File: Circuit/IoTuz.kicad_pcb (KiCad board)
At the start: 2 copper layers, 150 x 95 mm, 103 parts, among them J1 Jack.3.5mm-Mono, P1 ALLIGATOR_X39, P2 BATTERY, P3 USB_5PIN_SHELL, P4 LED_1, P5 LED_2, P8 IRReceiver, Q1 S8050, Q2 S8050, Q202 FDN340P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

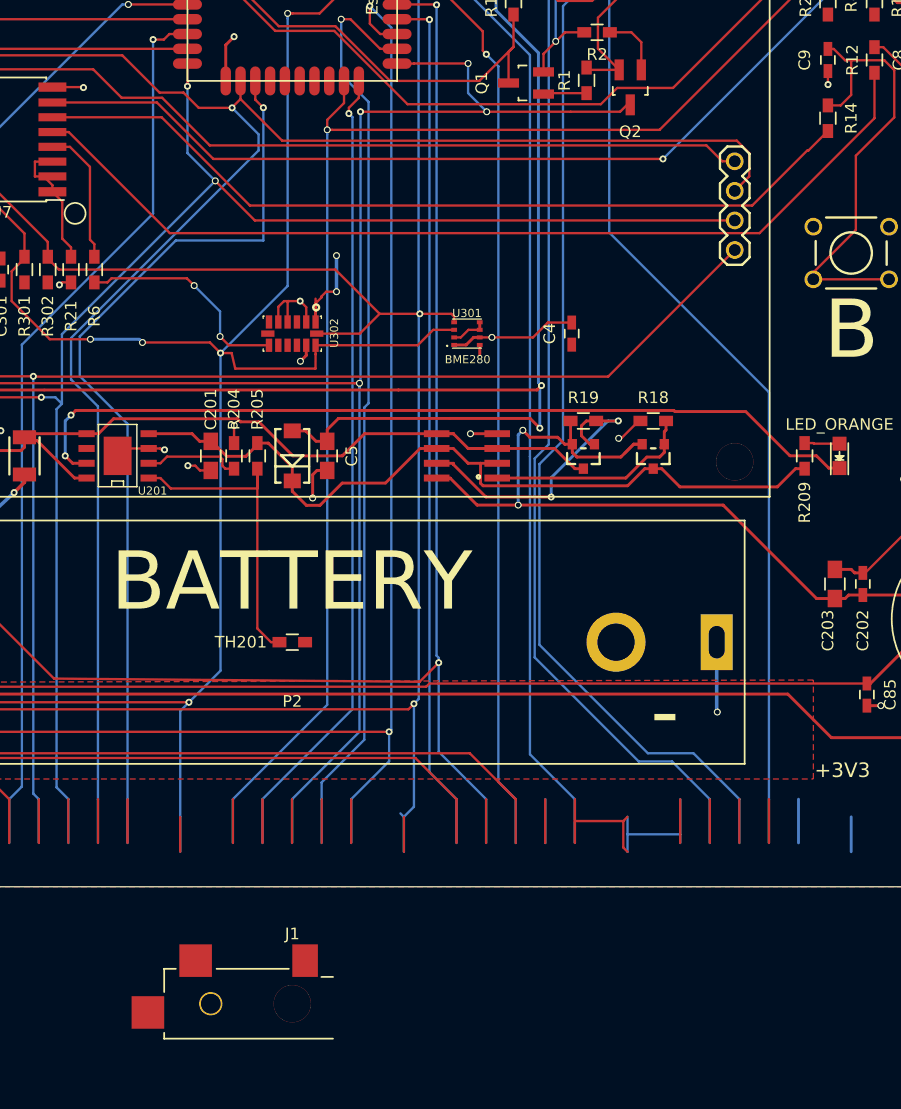
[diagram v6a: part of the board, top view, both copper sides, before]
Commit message: BOM changes to fix #15, fix #24.
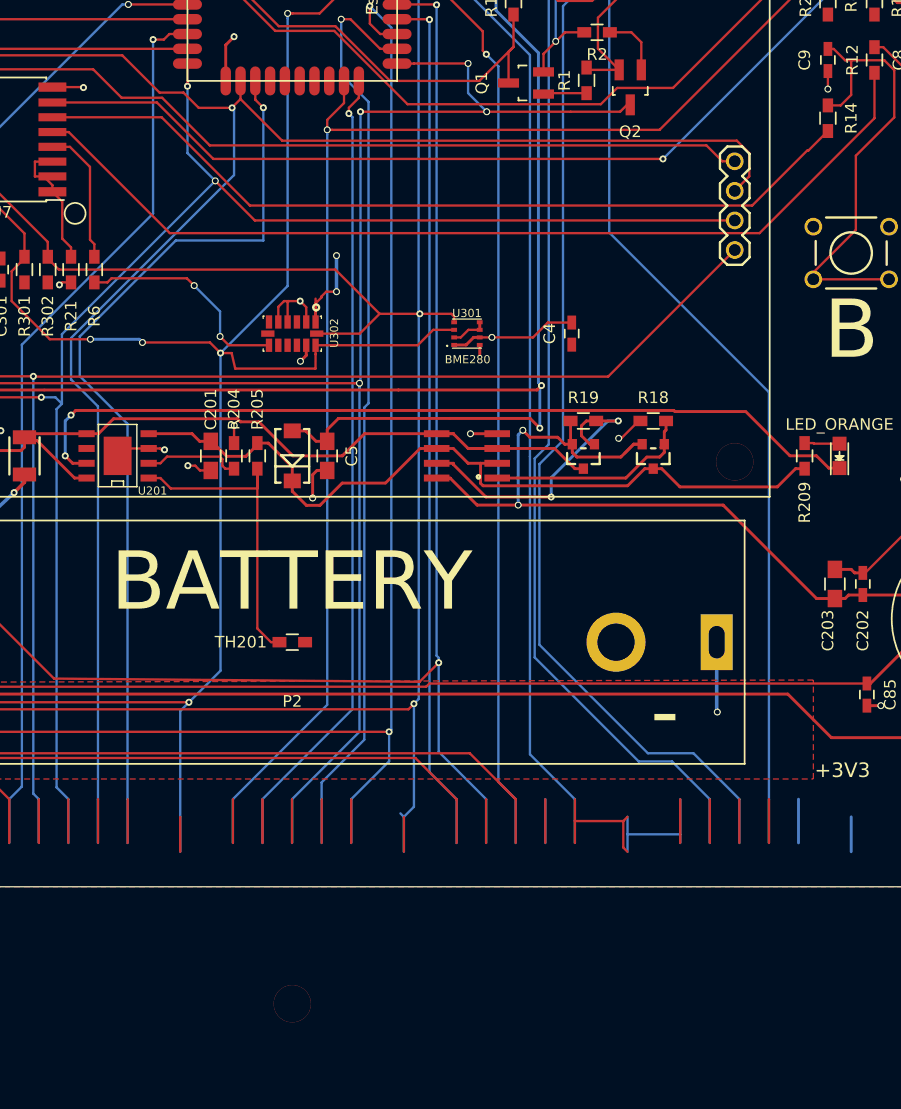
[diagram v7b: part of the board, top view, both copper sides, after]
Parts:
- removed J1: Jack.3.5mm-Mono, libs:3.5mmMonoTSJack.MJ-3523-SMT.Switch
- R16: value 22R -> 22R 1/4W
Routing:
- net /IO13: track 196.5 -> 194.7 mm
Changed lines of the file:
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@@
   (general
     (links 391)
-    (no_connects 55)
+    (no_connects 51)
     (area 49.949999 54.949999 200.050001 150.050001)
     (thickness 1.6)
     (drawings 219)
-    (tracks 1398)
+    (tracks 1397)
     (zones 0)
-    (modules 103)
+    (modules 102)
     (nets 122)
   )
@@
       (effects (font (size 1 1) (thickness 0.15)))
     )
-    (fp_text value 22R (at 0 1.9 90) (layer F.Fab)
+    (fp_text value "22R 1/4W" (at 0 1.9 90) (layer F.Fab)
       (effects (font (size 1 1) (thickness 0.15)))
     )
@@
     )
   )
-  (module libs:3.5mmMonoTSJack.MJ-3523-SMT.Switch (layer F.Cu)
-    (at 125 160.050001)
-    (fp_text reference J1 (at 0 -6) (layer F.SilkS)
-      (effects (font (size 1 1) (thickness 0.15)))
-    )
-    (fp_text value Jack.3.5mm-Mono (at 0 4.75) (layer F.Fab)
-      (effects (font (size 1 1) (thickness 0.15)))
-    )
-    (fp_text user "Keep Clear - Insertion Point" (at 18 0) (layer Cmts.User)
-      (effects (font (size 1 1) (thickness 0.15)))
-    )
-    (fp_line (start 3.5 -3.25) (end 3.5 3.25) (layer Cmts.User) (width 0.15))
-    (fp_text user Overhang (at 4.75 0 90) (layer Cmts.User)
-      (effects (font (size 1 1) (thickness 0.15)))
-    )
-    (fp_line (start 6.25 3.25) (end -11.25 3.25) (layer F.CrtYd) (width 0.15))
-    (fp_line (start 6.25 -3.25) (end 6.25 3.25) (layer F.CrtYd) (width 0.15))
-    (fp_line (start -11.25 -3.25) (end 6.25 -3.25) (layer F.CrtYd) (width 0.15))
-    (fp_line (start -11.25 3.25) (end -11.25 -3.25) (layer F.CrtYd) (width 0.15))
-    (fp_line (start 3.5 -2.3) (end 2.5 -2.3) (layer F.SilkS) (width 0.15))
-    (fp_line (start -6.5 -3) (end -0.3 -3) (layer F.SilkS) (width 0.15))
-    (fp_line (start -11 -3) (end -10 -3) (layer F.SilkS) (width 0.15))
-    (fp_line (start -11 -1) (end -11 -3) (layer F.SilkS) (width 0.15))
-    (fp_line (start -11 3) (end -11 2.5) (layer F.SilkS) (width 0.15))
-    (fp_line (start 3.5 3) (end -11 3) (layer F.SilkS) (width 0.15))
-    (pad "" thru_hole circle (at 0 0) (size 2 2) (drill 1.7) (layers *.Cu *.Mask))
-    (pad "" thru_hole circle (at -7 0) (size 2 2) (drill 1.7) (layers *.Cu *.Mask))
-    (pad 1 smd rect (at 1.1 -3.7) (size 2.2 2.8) (layers F.Cu F.Paste F.Mask)
-      (net 2 GND))
-    (pad 2 smd rect (at -8.3 -3.7) (size 2.8 2.8) (layers F.Cu F.Paste F.Mask)
-      (net 99 /MonoAudioOut))
-    (pad 10 smd rect (at -12.4 0.75) (size 2.8 2.8) (layers F.Cu F.Paste F.Mask)
-      (net 94 "Net-(J1-Pad10)"))
-  )
   (gr_text "© 2016 Robert Powers\nLicense TAPR OHL v1.0" (at 70 136.5) (layer F.SilkS)
     (effects (font (size 1.25 1.25) (thickness 0.25)))
@@
   (segment (start 86 62.9) (end 85.9004 62.9) (width 0.2032) (layer F.Cu) (net 1) (status 30))
   (segment (start 100 95.9) (end 100 96.05) (width 0.2032) (layer F.Cu) (net 1) (status 30))
+  (via (at 171 81.5) (size 0.6) (drill 0.4) (layers F.Cu B.Cu) (net 2))
+  (segment (start 171 81.5) (end 171 79.95) (width 0.2032) (layer F.Cu) (net 2))
   (segment (start 145.675 102.825) (end 146.95 101.55) (width 0.2032) (layer F.Cu) (net 2))
   (segment (start 146.95 101.55) (end 149 101.55) (width 0.2032) (layer F.Cu) (net 2))
@@
   (via (at 62.5652 114.012) (size 0.6) (layers F.Cu B.Cu) (net 2))
   (via (at 193.292 133.738) (size 0.6) (layers F.Cu B.Cu) (net 2))
-  (via (at 171.012 81.1125) (size 0.6) (layers F.Cu B.Cu) (net 2))
   (via (at 177.602 77.1926) (size 0.6) (layers F.Cu B.Cu) (net 2))
   (via (at 60.6152 98.9357) (size 0.6) (layers F.Cu B.Cu) (net 2))
@@
   (segment (start 192.68 134.05) (end 192.993 133.738) (width 0.2032) (layer F.Cu) (net 2))
   (segment (start 192 134.05) (end 192.68 134.05) (width 0.2032) (layer F.Cu) (net 2) (status 10))
-  (segment (start 171 81.1004) (end 171 79.95) (width 0.2032) (layer F.Cu) (net 2) (status 20))
-  (segment (start 171.012 81.1125) (end 171 81.1004) (width 0.2032) (layer F.Cu) (net 2))
   (segment (start 64.0667 106.687) (end 64.15 106.77) (width 0.2032) (layer F.Cu) (net 2) (status 30))
   (segment (start 62.7152 106.687) (end 64.0667 106.687) (width 0.2032) (layer F.Cu) (net 2) (status 20))
@@
   (segment (start 104.659 107.97) (end 105.215 108.526) (width 0.2032) (layer B.Cu) (net 25))
   (segment (start 103.446 107.97) (end 104.659 107.97) (width 0.2032) (layer B.Cu) (net 25))
+  (segment (start 119.832 83.1096) (end 120 83.2776) (width 0.2032) (layer B.Cu) (net 26))
+  (segment (start 120 83.2776) (end 120 88.880648) (width 0.2032) (layer B.Cu) (net 26))
+  (segment (start 120 88.880648) (end 106 102.880648) (width 0.2032) (layer B.Cu) (net 26))
+  (segment (start 106 102.880648) (end 106 106.438) (width 0.2032) (layer B.Cu) (net 26))
+  (segment (start 108.312 108.75) (end 108.312 142.484) (width 0.2032) (layer B.Cu) (net 26))
+  (segment (start 106 106.438) (end 108.312 108.75) (width 0.2032) (layer B.Cu) (net 26))
+  (segment (start 108.312 142.484) (end 108.312 146.242) (width 0.2032) (layer B.Cu) (net 26))
   (segment (start 163 90.24) (end 164.25 88.99) (width 0.2032) (layer F.Cu) (net 26))
   (segment (start 164.25 87) (end 163.1801 85.9301) (width 0.2032) (layer F.Cu) (net 26))
@@
   (segment (start 163.1801 85.9301) (end 124.13 85.9301) (width 0.2032) (layer F.Cu) (net 26))
   (segment (start 124.13 85.9301) (end 120.555 82.3551) (width 0.2032) (layer F.Cu) (net 26))
-  (segment (start 119.832 83.1096) (end 122.106 85.3834) (width 0.2032) (layer B.Cu) (net 26))
-  (segment (start 122.106 85.3834) (end 122.106 86.774648) (width 0.2032) (layer B.Cu) (net 26))
-  (segment (start 122.106 86.774648) (end 106 102.880648) (width 0.2032) (layer B.Cu) (net 26))
-  (segment (start 108.312 108.75) (end 108.312 142.484) (width 0.2032) (layer B.Cu) (net 26) (status 20))
-  (segment (start 106 102.880648) (end 106 106.438) (width 0.2032) (layer B.Cu) (net 26))
-  (segment (start 106 106.438) (end 108.312 108.75) (width 0.2032) (layer B.Cu) (net 26))
   (segment (start 82.772396 88.472396) (end 85.170542 88.472396) (width 0.2032) (layer B.Cu) (net 26))
   (segment (start 82 87.7) (end 82.772396 88.472396) (width 0.2032) (layer B.Cu) (net 26) (status 10))
@@
   (segment (start 82 102.94) (end 80.8572 104.083) (width 0.2032) (layer B.Cu) (net 26) (status 10))
   (segment (start 120.555 80.8) (end 120.555 82.3551) (width 0.2032) (layer F.Cu) (net 26) (status 10))
-  (segment (start 108.312 146.242) (end 108.312 142.484) (width 0.2032) (layer B.Cu) (net 26) (status 30))
   (segment (start 119.832 83.0784) (end 120.555 82.3551) (width 0.2032) (layer F.Cu) (net 26))
   (segment (start 119.832 83.1096) (end 119.832 83.0784) (width 0.2032) (layer F.Cu) (net 26))

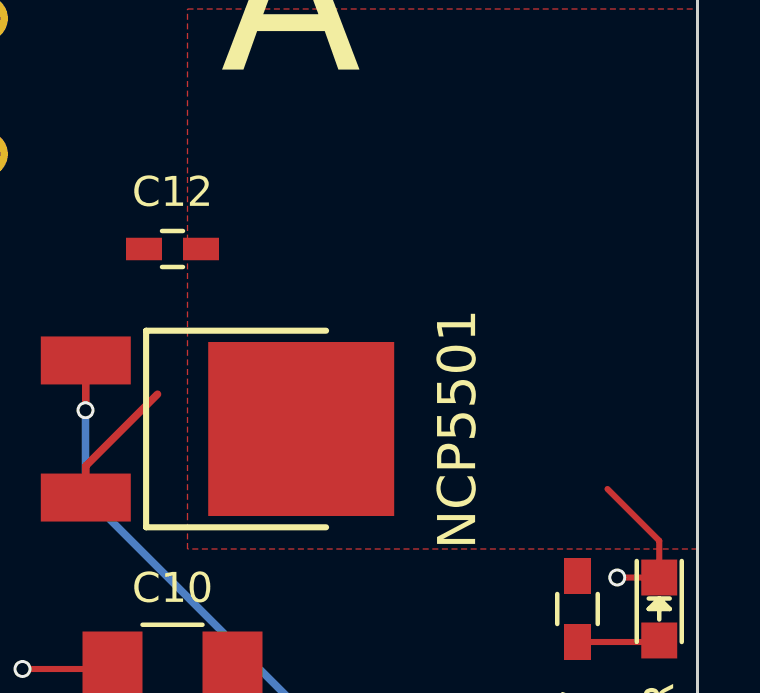
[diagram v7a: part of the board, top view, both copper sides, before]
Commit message: Put via stitching back on LDO to fix #23.
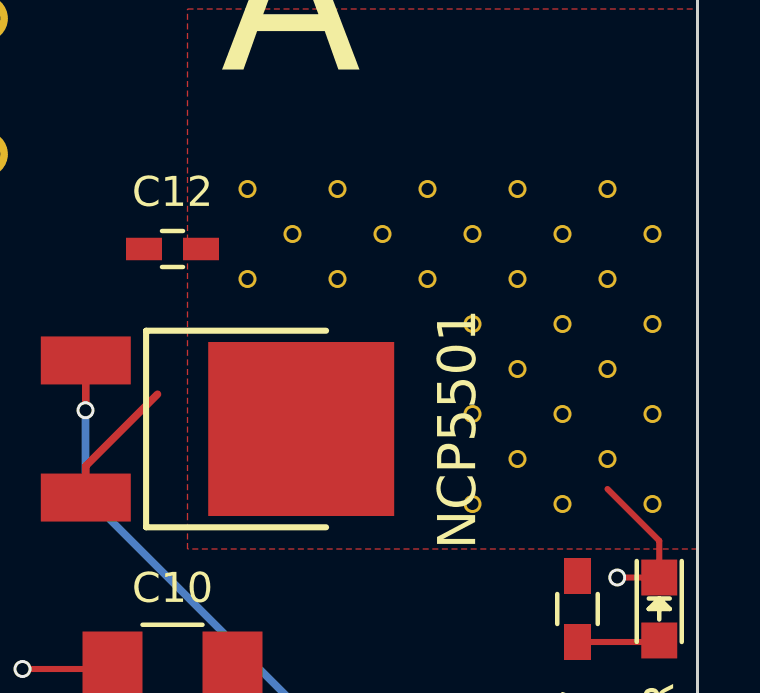
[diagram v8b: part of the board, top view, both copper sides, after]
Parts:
- added REF**: via.0.6mm-drill.0.4mm, libs:via.0.6mm-drill.0.4mm, F.Cu at (185.0, 102.0)
- added REF**: via.0.6mm-drill.0.4mm, libs:via.0.6mm-drill.0.4mm, F.Cu at (194.0, 99.0)
- added REF**: via.0.6mm-drill.0.4mm, libs:via.0.6mm-drill.0.4mm, F.Cu at (195.5, 100.5)
- added REF**: via.0.6mm-drill.0.4mm, libs:via.0.6mm-drill.0.4mm, F.Cu at (197.0, 99.0)
- added REF**: via.0.6mm-drill.0.4mm, libs:via.0.6mm-drill.0.4mm, F.Cu at (198.5, 100.5)
- added REF**: via.0.6mm-drill.0.4mm, libs:via.0.6mm-drill.0.4mm, F.Cu at (194.0, 102.0)
- added REF**: via.0.6mm-drill.0.4mm, libs:via.0.6mm-drill.0.4mm, F.Cu at (192.5, 103.5)
- added REF**: via.0.6mm-drill.0.4mm, libs:via.0.6mm-drill.0.4mm, F.Cu at (195.5, 103.5)
- added REF**: via.0.6mm-drill.0.4mm, libs:via.0.6mm-drill.0.4mm, F.Cu at (197.0, 102.0)
- added REF**: via.0.6mm-drill.0.4mm, libs:via.0.6mm-drill.0.4mm, F.Cu at (198.5, 103.5)
- added REF**: via.0.6mm-drill.0.4mm, libs:via.0.6mm-drill.0.4mm, F.Cu at (194.0, 105.0)
- added REF**: via.0.6mm-drill.0.4mm, libs:via.0.6mm-drill.0.4mm, F.Cu at (185.0, 99.0)
- added REF**: via.0.6mm-drill.0.4mm, libs:via.0.6mm-drill.0.4mm, F.Cu at (192.5, 106.5)
- added REF**: via.0.6mm-drill.0.4mm, libs:via.0.6mm-drill.0.4mm, F.Cu at (195.5, 106.5)
- added REF**: via.0.6mm-drill.0.4mm, libs:via.0.6mm-drill.0.4mm, F.Cu at (197.0, 105.0)
- added REF**: via.0.6mm-drill.0.4mm, libs:via.0.6mm-drill.0.4mm, F.Cu at (198.5, 106.5)
- added REF**: via.0.6mm-drill.0.4mm, libs:via.0.6mm-drill.0.4mm, F.Cu at (198.5, 109.5)
- added REF**: via.0.6mm-drill.0.4mm, libs:via.0.6mm-drill.0.4mm, F.Cu at (195.5, 109.5)
- added REF**: via.0.6mm-drill.0.4mm, libs:via.0.6mm-drill.0.4mm, F.Cu at (197.0, 108.0)
- added REF**: via.0.6mm-drill.0.4mm, libs:via.0.6mm-drill.0.4mm, F.Cu at (194.0, 108.0)
- added REF**: via.0.6mm-drill.0.4mm, libs:via.0.6mm-drill.0.4mm, F.Cu at (192.5, 109.5)
- added REF**: via.0.6mm-drill.0.4mm, libs:via.0.6mm-drill.0.4mm, F.Cu at (191.0, 99.0)
- added REF**: via.0.6mm-drill.0.4mm, libs:via.0.6mm-drill.0.4mm, F.Cu at (186.5, 100.5)
- added REF**: via.0.6mm-drill.0.4mm, libs:via.0.6mm-drill.0.4mm, F.Cu at (188.0, 102.0)
- added REF**: via.0.6mm-drill.0.4mm, libs:via.0.6mm-drill.0.4mm, F.Cu at (188.0, 99.0)
- added REF**: via.0.6mm-drill.0.4mm, libs:via.0.6mm-drill.0.4mm, F.Cu at (189.5, 100.5)
- added REF**: via.0.6mm-drill.0.4mm, libs:via.0.6mm-drill.0.4mm, F.Cu at (192.5, 100.5)
- added REF**: via.0.6mm-drill.0.4mm, libs:via.0.6mm-drill.0.4mm, F.Cu at (191.0, 102.0)
